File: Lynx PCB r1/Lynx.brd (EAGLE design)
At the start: 124.3 x 53.1 mm, 111 parts, among them IC1 LM321MF, IC3 ICL7660, Q1 8MHz

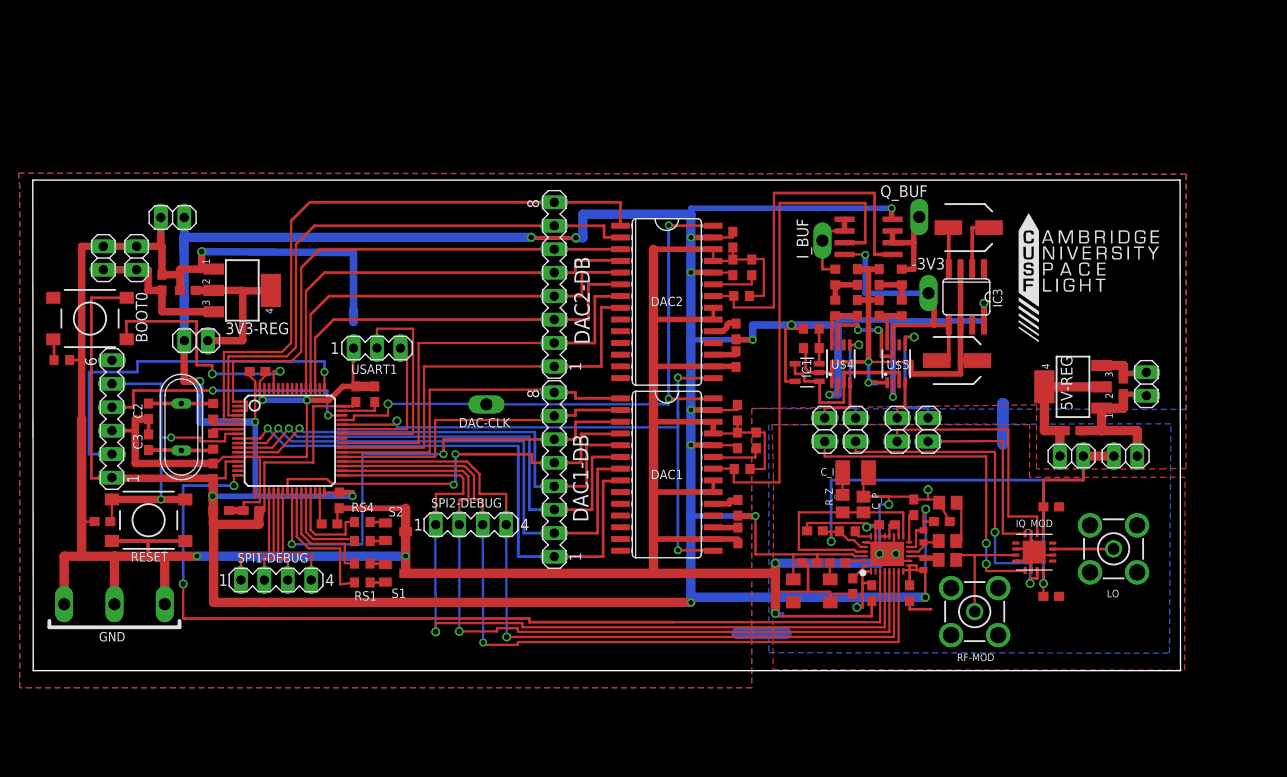
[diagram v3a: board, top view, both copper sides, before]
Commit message: Changes as per Cillian
Changed the layout of the RF
swapped out the coax connectors
added "TUNE" test point
revamped the ground planes
stitched the ground planes (a lot)
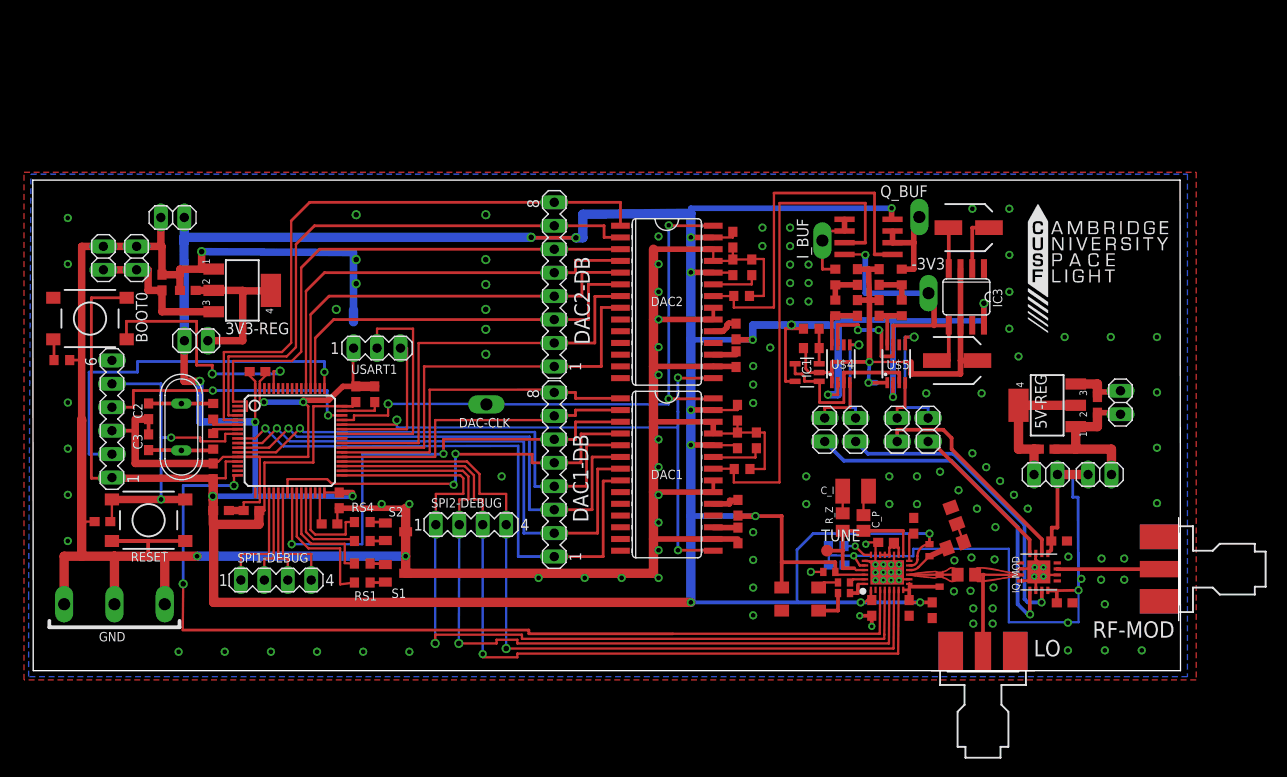
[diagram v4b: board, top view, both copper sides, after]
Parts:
- added TUNE: PTR1B1,27, testpad:B1,27
- C31, C6, C7: device rcl:C0603 -> rcl:C0402
- LO, RF-MOD: value BU-SMA-V -> SMA-142-0711-821/826; device con-coax:BU-SMA-V -> con-coax:J502-ND-142-0711-821/826
- moved RF-MOD 22.6 mm to (124.1, 11.0)
- moved LO 19.4 mm to (102.9, 0.00), turned to 90 degrees
- moved C33 9.66 mm to (97.4, 6.55), turned to 270 degrees
- moved C29 4.38 mm to (87.0, 11.4), flipped to the bottom
- moved C14 3.80 mm to (111.2, 14.1)
- moved 5V-REG 3.44 mm to (109.8, 28.8)
- moved C43 3.44 mm to (109.8, 24.0)
- moved C44 3.44 mm to (115.3, 28.8)
- moved JP10 3.44 mm to (117.8, 29.1)
- moved JP2 3.44 mm to (109.7, 21.2)
- moved JP4 3.44 mm to (115.5, 21.2)
- moved C5 2.60 mm to (101.1, 10.4)
- moved L1 2.51 mm to (98.2, 9.75)
- moved C31 2.37 mm to (86.2, 10.7)
- moved C6 2.25 mm to (87.8, 9.56)
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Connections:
- net N$9 renamed RF+
- net GND: now also LO.G@1, LO.G@2, LO.G@3, LO.G@4, RF-MOD.G@1, RF-MOD.G@2, RF-MOD.G@3, RF-MOD.G@4; no longer LO.2, LO.3, LO.4, LO.5, RF-MOD.2, RF-MOD.3, RF-MOD.4, RF-MOD.5
- net LO: now also LO.1; no longer RF-MOD.1
- net N$1: now also TUNE.TP
- net RF-MOD: now also RF-MOD.1; no longer LO.1
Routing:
- net GND: track 586.9 -> 483.4 mm, vias 14 -> 135
- net N$8: track 3.37 -> 12.0 mm
- net LO: track 12.8 -> 21.1 mm
- net N$1: track 25.2 -> 17.4 mm
- net +3V3: track 515.2 -> 522.3 mm
- net RF-MOD: track 6.62 -> 11.1 mm
- net BBPI: track 27.7 -> 24.1 mm
- net BBMI: track 20.6 -> 16.9 mm
- net BBPQ: track 37.0 -> 33.4 mm, vias 2 -> 1
- net N$10: track 5.20 -> 2.11 mm
- net +5V: track 73.2 -> 75.7 mm
- net BBMQ: track 35.8 -> 37.5 mm, vias 2 -> 1
- net N$30: track 1.99 -> 3.30 mm, vias 0 -> 1
- net RF+: track 4.04 -> 4.84 mm
- net SPI2-MISO: track 87.0 -> 87.7 mm
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- added copper zone on layer 1, net LO
- added copper zone on layer 1, net N$8

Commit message: Final PCB r1 commit
Fixed lots of little thing.
Gerbers checked
Fixed 0.54v generation oopsie (inverting and non-inverting terminals
wrong way around)
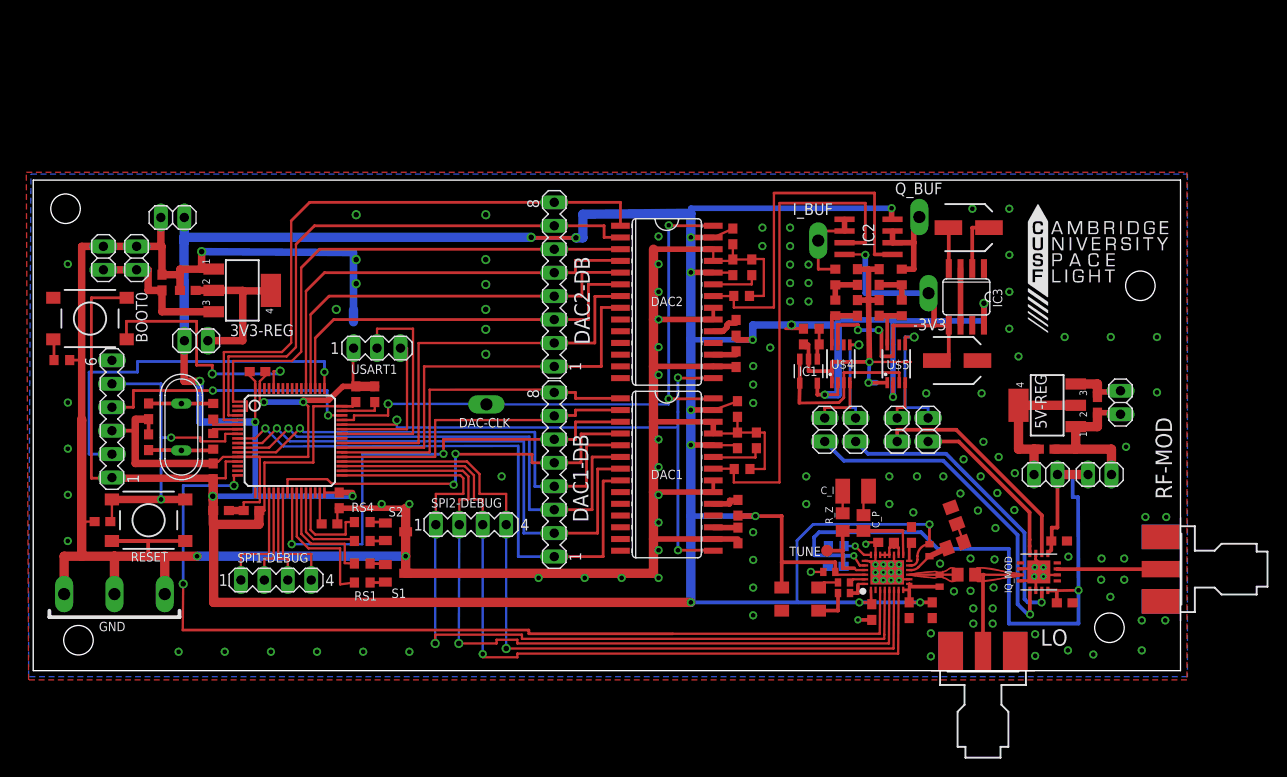
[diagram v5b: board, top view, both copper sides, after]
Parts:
- moved GND 1.10 mm to (14.2, 8.30)
- moved GND1 1.10 mm to (8.80, 8.30)
- moved GND2 1.10 mm to (3.35, 8.30)
- moved C34 1.03 mm to (95.2, 14.7)
- moved I_BUF 0.45 mm to (85.0, 46.6)
- moved C32 0.45 mm to (90.8, 6.35)
- moved C25 0.40 mm to (76.3, 28.4)
- moved C10 0.40 mm to (76.2, 37.1)
- moved R12 0.40 mm to (84.3, 35.4)
- moved C27 0.35 mm to (75.8, 47.0)
- moved C30 0.25 mm to (94.9, 6.55)
- moved IC1 0.21 mm to (84.0, 32.5), turned to 180 degrees
- moved RF-MOD 0.20 mm to (124.3, 11.0)
- moved C29 0.18 mm to (87.0, 11.3), turned to 180 degrees
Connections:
- net +0.54V: now also IC1.3; no longer IC1.1
- net N$42: now also IC1.1; no longer IC1.3
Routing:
- net GND: track 483.4 -> 466.7 mm, vias 135 -> 140
- net +5V: track 75.7 -> 84.1 mm
- net BBMI: track 16.9 -> 18.6 mm
- net N$33: track 3.44 -> 2.08 mm
- net +3V3: track 522.3 -> 521.1 mm
- net I_BUF: track 9.21 -> 10.1 mm
- net BBPI: track 24.1 -> 24.9 mm
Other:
- outline, holes or cut-outs redrawn

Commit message: What was send to the board house
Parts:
- moved C7 0.87 mm to (87.8, 7.54), turned to 90 degrees
- moved C31 0.15 mm to (86.2, 10.8)
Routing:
- net GND: track 466.7 -> 462.8 mm
- net N$3: track 2.61 -> 3.15 mm
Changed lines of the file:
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@@
 </element>
 <element name="C6" library="rcl" package="C0402" value="470pf" x="87.842025" y="9.558578125" smashed="yes">
-<attribute name="VALUE" x="89.227028125" y="7.813578125" size="0.8128" layer="27" font="vector" ratio="12" rot="R180"/>
-</element>
-<element name="C7" library="rcl" package="C0402" value="470pf" x="87.842025" y="8.40858125" smashed="yes"/>
+<attribute name="VALUE" x="86.186421875" y="9.227028125" size="0.8128" layer="27" font="vector" ratio="12" rot="R270"/>
+</element>
+<element name="C7" library="rcl" package="C0402" value="470pf" x="87.84141875" y="7.542025" smashed="yes" rot="R90"/>
 <element name="10MHZ" library="Lynx components" package="TXCO5.6" value="TCXO" x="83.092028125" y="7.75858125">
 <attribute name="FREQUENCY" value="" x="83.092028125" y="7.75858125" size="1.778" layer="27" display="off"/>
@@
 <attribute name="VALUE" x="94.295" y="5.185" size="0.8128" layer="27" font="vector" ratio="12" rot="R270"/>
 </element>
-<element name="C31" library="rcl" package="C0402" value="0.01uF" x="86.25" y="10.7" smashed="yes" rot="R180">
-<attribute name="ARM" x="86.25" y="10.7" size="0.8128" layer="27" rot="R180" display="off"/>
-<attribute name="VALUE" x="88.135" y="12.155" size="0.8128" layer="27" font="vector" ratio="12" rot="R180"/>
+<element name="C31" library="rcl" package="C0402" value="0.01uF" x="86.25" y="10.85" smashed="yes" rot="R180">
+<attribute name="ARM" x="86.25" y="10.85" size="0.8128" layer="27" rot="R180" display="off"/>
+<attribute name="VALUE" x="88.135" y="12.305" size="0.8128" layer="27" font="vector" ratio="12" rot="R180"/>
 </element>
 <element name="C32" library="rcl" package="C0603" value="0.01uF" x="90.85" y="6.35" smashed="yes" rot="R270">
@@
 <wire x1="91.26" y1="13.9" x2="90.4" y2="13.9" width="0.254" layer="1"/>
 <wire x1="90.4" y1="13.9" x2="90.2" y2="13.7" width="0.254" layer="1"/>
-<wire x1="85.092028125" y1="6.50858125" x2="87.192025" y2="6.50858125" width="0.4064" layer="1"/>
-<wire x1="87.192025" y1="6.50858125" x2="87.192025" y2="8.40858125" width="0.4064" layer="1"/>
-<wire x1="85.6" y1="10.7" x2="84.35" y2="10.7" width="0.254" layer="1"/>
+<wire x1="85.6" y1="10.85" x2="84.35" y2="10.7" width="0.254" layer="1"/>
 <via x="90.2" y="13.7" extent="1-16" drill="0.4"/>
 <polygon width="0.4064" layer="16" isolate="0.4064" orphans="yes">
@@
 <wire x1="90.85" y1="7.2" x2="90.76" y2="7.65" width="0.254" layer="1"/>
 <wire x1="90.76" y1="7.65" x2="90.76" y2="8.75" width="0.254" layer="1"/>
-<wire x1="86.9" y1="10.7" x2="87.1" y2="10.4" width="0.254" layer="1"/>
+<wire x1="86.9" y1="10.85" x2="87.1" y2="10.4" width="0.254" layer="1"/>
 <wire x1="87.1" y1="10.4" x2="90.11" y2="10.4" width="0.254" layer="1"/>
 <wire x1="81.092028125" y1="9.00858125" x2="81.092028125" y2="11.75" width="0.4064" layer="1"/>
 <wire x1="81.092028125" y1="11.75" x2="81.092028125" y2="16.75" width="0.4064" layer="1"/>
 <wire x1="81.092028125" y1="16.75" x2="78.25" y2="16.75" width="0.4064" layer="1"/>
-<wire x1="86.9" y1="10.7" x2="86.9" y2="11.75" width="0.4064" layer="1"/>
+<wire x1="86.9" y1="10.85" x2="86.9" y2="11.75" width="0.4064" layer="1"/>
 <wire x1="86.9" y1="11.75" x2="81.092028125" y2="11.75" width="0.4064" layer="1"/>
 <wire x1="94.91" y1="11.4" x2="95.16360625" y2="11.4" width="0.254" layer="1"/>
@@
 <contactref element="C7" pad="2"/>
 <contactref element="U$3" pad="28"/>
-<wire x1="88.492025" y1="8.40858125" x2="89.35" y2="8.40858125" width="0.4064" layer="1"/>
-<wire x1="89.35" y1="8.40858125" x2="89.35" y2="9.3" width="0.4064" layer="1"/>
+<wire x1="87.84141875" y1="8.192025" x2="88.8204875" y2="8.20276875" width="0.4064" layer="1"/>
+<wire x1="88.8204875" y1="8.20276875" x2="89.35" y2="8.738125" width="0.4064" layer="1"/>
+<wire x1="89.35" y1="8.738125" x2="89.35" y2="9.3" width="0.4064" layer="1"/>
 <wire x1="89.35" y1="9.3" x2="89.35" y2="9.4" width="0.254" layer="1"/>
 <wire x1="89.35" y1="9.4" x2="90.11" y2="9.4" width="0.254" layer="1"/>
